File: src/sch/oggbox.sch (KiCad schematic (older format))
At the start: 146 parts, among them IC1 VS1053, IC2 MCP73831T, IC3 SD_CARD, IC4 MCP1802T-3002I-OT, IC5 STM32F103RBT, IC7 TPS76318, IC8 TPS76328, IC9 MCP102, P10 PHONES, P2 USB, P5 CONN_4, P6 CONN_28, P7 FTDI, P8 JTAG, P9 LINE, Q1 BC817, Q2 BC817, Q3 BSH121, Q4 BSH121, Q5 BSH121, SW1 VOL_UP, SW10 UP, SW11 HOLD, SW2 VOL_DN, SW3 RESET, SW4 MENU, SW5 SET, SW7 DOWN, SW8 LEFT, SW9 RIGHT, X1 12.288MHz, X2 32768Hz, X3 8MHz

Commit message: Routed the new volume switches
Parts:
- removed SW1: VOL_UP, SW_B3U-3000P-B, symbol SW_PUSH
- removed SW2: VOL_DN, SW_B3U-3000P-B, symbol SW_PUSH
- removed SW3: RESET, SW_B3U-3000P-B, symbol SW_PUSH
- added SW1: VOL_UP, symbol SW_PUSH4
- added SW2: VOL_DN, symbol SW_PUSH4
- added SW3: RESET, symbol SW_PUSH4
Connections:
- wire segments 526 -> 536
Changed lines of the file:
@@
-EESchema Schematic File Version 2  date Sat 22 Sep 2012 20:59:45 BST
+EESchema Schematic File Version 2  date Sun 23 Sep 2012 13:00:38 BST
 LIBS:power
 LIBS:device
@@
 Sheet 1 1
 Title "OggBox open hardware media player"
-Date "22 sep 2012"
+Date "23 sep 2012"
 Rev "B"
 Comp "nathandumont.com"
@@
 Comment4 ""
 $EndDescr
-Text Label 10250 10500 1    60   ~ 0
-RBG
+Wire Wire Line
+	8250 2700 8650 2700
+Wire Wire Line
+	8250 2700 8250 2600
+Connection ~ 5500 4050
+Wire Wire Line
+	5500 4050 5500 3950
+Wire Wire Line
+	5500 3950 5600 3950
+Connection ~ 6300 4150
+Wire Wire Line
+	6200 4250 6300 4250
+Wire Wire Line
+	6300 4250 6300 4150
 Wire Wire Line
 	10250 10300 10250 10550
@@
 	8350 2600 8350 2800
 Wire Wire Line
-	8350 2700 8650 2700
-Wire Wire Line
 	8650 2700 8650 2450
 Connection ~ 8350 1900
@@
 	8350 2000 8350 1800
 Wire Wire Line
-	8350 1900 9550 1900
-Wire Wire Line
-	9550 1900 9550 2650
+	9550 2650 9550 1900
 Connection ~ 8650 1900
 Wire Wire Line
@@
 Wire Wire Line
 	10250 9700 9350 9700
+Wire Wire Line
+	6200 3950 6300 3950
+Wire Wire Line
+	6300 3950 6300 4050
+Connection ~ 6300 4050
+Wire Wire Line
+	5500 4150 5500 4250
+Wire Wire Line
+	5500 4250 5600 4250
+Connection ~ 5500 4150
+Wire Wire Line
+	9550 1900 8250 1900
+Wire Wire Line
+	8250 1900 8250 2000
+$Comp
+L SW_PUSH4 SW3
+U 1 1 505EF9B9
+P 8300 2300
+F 0 "SW3" H 8450 2460 50  0000 C CNN
+F 1 "RESET" H 8300 2170 50  0000 C CNN
+	1    8300 2300
+	0    -1   -1   0
+$EndComp
+$Comp
+L SW_PUSH4 SW?
+U 1 1 505EF927
+P 5900 4000
+AR Path="/505EF91E" Ref="SW?"  Part="1"
+AR Path="/505EF927" Ref="SW1"  Part="1"
+F 0 "SW1" H 5550 4100 50  0000 C CNN
+F 1 "VOL_UP" H 6300 4100 50  0000 C CNN
+	1    5900 4000
+	1    0    0    -1
+$EndComp
+$Comp
+L SW_PUSH4 SW2
+U 1 1 505EF91E
+P 5900 4200
+F 0 "SW2" H 6050 4360 50  0000 C CNN
+F 1 "VOL_DN" H 5700 4350 50  0000 C CNN
+	1    5900 4200
+	1    0    0    1
+$EndComp
+Text Label 10250 10500 1    60   ~ 0
+RBG
 $Comp
 L C C?
@@
 U 1 1 4F3E5CAC
 P 5700 3650
-F 0 "D1" V 5450 3650 60  0000 C CNN
+F 0 "D1" V 5700 3850 60  0000 C CNN
 F 1 "LED_RG" V 5950 3650 60  0000 C CNN
 F 2 "SOT23" V 6050 3650 60  0001 C CNN
@@
 $EndComp
 $Comp
-L SW_PUSH SW3
-U 1 1 4D36058B
-P 8350 2300
-F 0 "SW3" H 8500 2410 50  0000 C CNN
-F 1 "RESET" H 8350 2220 50  0000 C CNN
-F 2 "SW_B3U-3000P-B" H 8350 2320 50  0001 C CNN
-F 4 "9962859" H 8350 2300 60  0001 C CNN "Farnell"
-	1    8350 2300
-	0    -1   -1   0
-$EndComp
-$Comp
 L R R?
 U 1 1 4D36040D
@@
 	1    0    0    -1
 $EndComp
-$Comp
-L SW_PUSH SW2
-U 1 1 4D35AE93
-P 5900 4150
-F 0 "SW2" H 6200 4200 50  0000 C CNN
-F 1 "VOL_DN" H 5500 4200 50  0000 C CNN
-F 2 "SW_B3U-3000P-B" H 5500 4300 50  0001 C CNN
-F 4 "9962859" H 5900 4150 60  0001 C CNN "Farnell"
-	1    5900 4150
-	1    0    0    -1
-$EndComp
-$Comp
-L SW_PUSH SW1
-U 1 1 4D35AE8C
-P 5900 4050
-F 0 "SW1" H 6200 4100 50  0000 C CNN
-F 1 "VOL_UP" H 5500 4100 50  0000 C CNN
-F 2 "SW_B3U-3000P-B" H 5500 4200 50  0001 C CNN
-F 4 "9962859" H 5900 4050 60  0001 C CNN "Farnell"
-	1    5900 4050
-	1    0    0    -1
-$EndComp

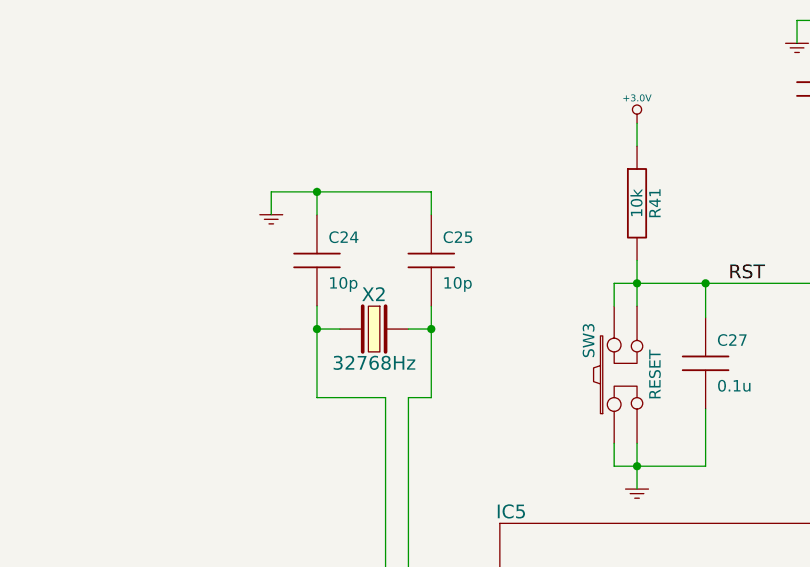
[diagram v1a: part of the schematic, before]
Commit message: Changed the footprint of the RTC crystal to an SMD part
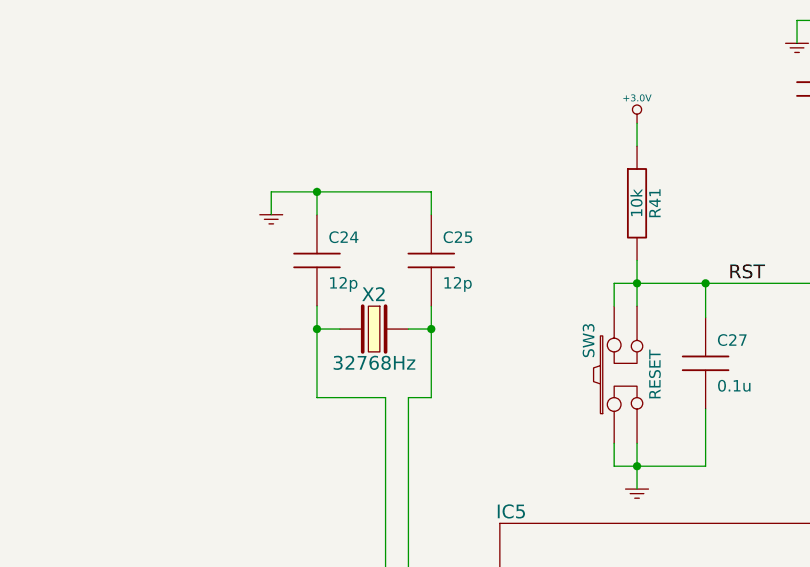
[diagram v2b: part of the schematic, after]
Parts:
- C24, C25: value 10p -> 12p
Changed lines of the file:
@@
-EESchema Schematic File Version 2  date Sun 23 Sep 2012 13:00:38 BST
+EESchema Schematic File Version 2  date Sun 23 Sep 2012 15:55:00 BST
 LIBS:power
 LIBS:device
@@
 AR Path="/4D35FD0D" Ref="C25"  Part="1"
 F 0 "C25" H 7500 1900 50  0000 L CNN
-F 1 "10p" H 7500 1700 50  0000 L CNN
+F 1 "12p" H 7500 1700 50  0000 L CNN
 F 2 "SM0805" H 7500 1800 50  0001 C CNN
 	1    7450 1800
@@
 P 6950 1800
 F 0 "C24" H 7000 1900 50  0000 L CNN
-F 1 "10p" H 7000 1700 50  0000 L CNN
+F 1 "12p" H 7000 1700 50  0000 L CNN
 F 2 "SM0805" H 7000 1800 50  0001 C CNN
 	1    6950 1800

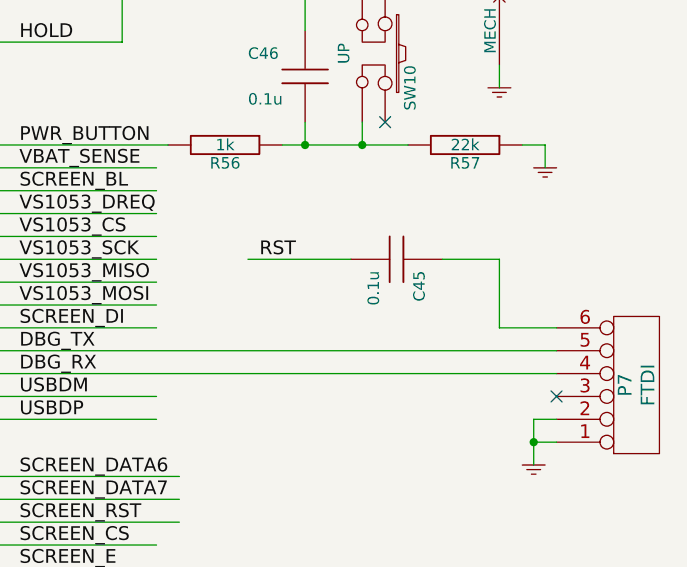
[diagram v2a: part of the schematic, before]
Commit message: Moving stuff around to try and shift the SD socket
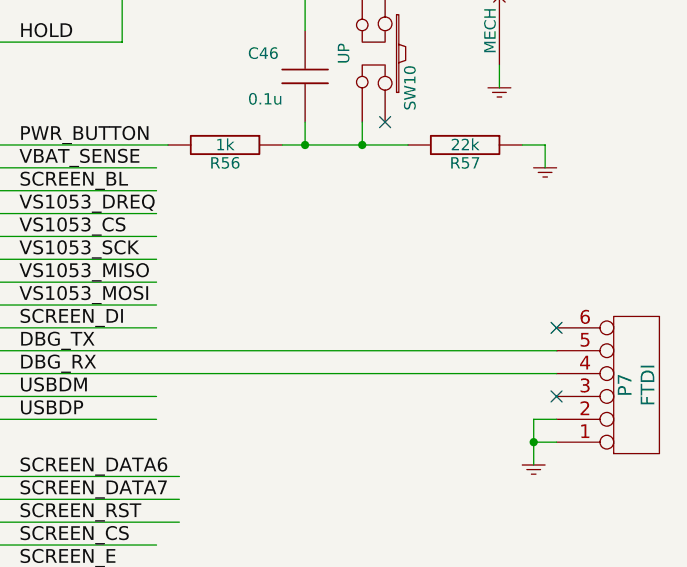
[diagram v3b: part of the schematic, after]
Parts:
- removed C45: 0.1u, SM0805, symbol C
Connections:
- wire segments 536 -> 532
- no-connect marks 19 -> 20
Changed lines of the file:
@@
-EESchema Schematic File Version 2  date Sun 23 Sep 2012 15:55:00 BST
+EESchema Schematic File Version 2  date Mon 24 Sep 2012 12:49:30 BST
+LIBS:74xx
+LIBS:adc-dac
+LIBS:analog_switches
+LIBS:atmel
+LIBS:audio
+LIBS:cmos4000
+LIBS:conn
+LIBS:contrib
+LIBS:cypress
+LIBS:dev_boards
+LIBS:device
+LIBS:digital-audio
+LIBS:display
+LIBS:dsp
+LIBS:intel
+LIBS:interface
+LIBS:linear
+LIBS:maxim
+LIBS:memory
+LIBS:microchip
+LIBS:microcontrollers
+LIBS:motorola
+LIBS:parallax
+LIBS:philips
 LIBS:power
-LIBS:device
+LIBS:regul
+LIBS:siliconi
+LIBS:special
+LIBS:texas
 LIBS:transistors
-LIBS:conn
-LIBS:linear
-LIBS:regul
-LIBS:74xx
-LIBS:cmos4000
-LIBS:adc-dac
-LIBS:memory
+LIBS:valves
 LIBS:xilinx
-LIBS:special
-LIBS:microcontrollers
-LIBS:dsp
-LIBS:microchip
-LIBS:analog_switches
-LIBS:motorola
-LIBS:texas
-LIBS:intel
-LIBS:audio
-LIBS:interface
-LIBS:digital-audio
-LIBS:philips
-LIBS:display
-LIBS:cypress
-LIBS:siliconi
-LIBS:opto
-LIBS:atmel
-LIBS:contrib
-LIBS:valves
 LIBS:oggbox-cache
 EELAYER 25  0
@@
 Sheet 1 1
 Title "OggBox open hardware media player"
-Date "23 sep 2012"
+Date "24 sep 2012"
 Rev "B"
 Comp "nathandumont.com"
@@
 Comment4 ""
 $EndDescr
+NoConn ~ 15500 4350
 Wire Wire Line
 	8250 2700 8650 2700
@@
 Wire Wire Line
 	13050 4550 15500 4550
-Wire Wire Line
-	15500 4350 15250 4350
-Wire Wire Line
-	15250 4350 15250 4050
-Wire Wire Line
-	15250 4050 15000 4050
 Wire Wire Line
 	6500 4900 6500 4800
@@
 Wire Wire Line
 	4300 3350 4300 3550
-Wire Wire Line
-	14600 4050 14150 4050
 Connection ~ 15400 4850
 Wire Wire Line
@@
 	1    0    0    -1
 $EndComp
-Text Label 14200 4050 0    60   ~ 0
-RST
-$Comp
-L C C45
-U 1 1 4F3E4BD3
-P 14800 4050
-F 0 "C45" H 14850 4150 50  0000 L CNN
-F 1 "0.1u" H 14850 3950 50  0000 L CNN
-F 2 "SM0805" H 14850 4050 50  0001 C CNN
-	1    14800 4050
-	0    1    1    0
-$EndComp
 NoConn ~ 15500 4650

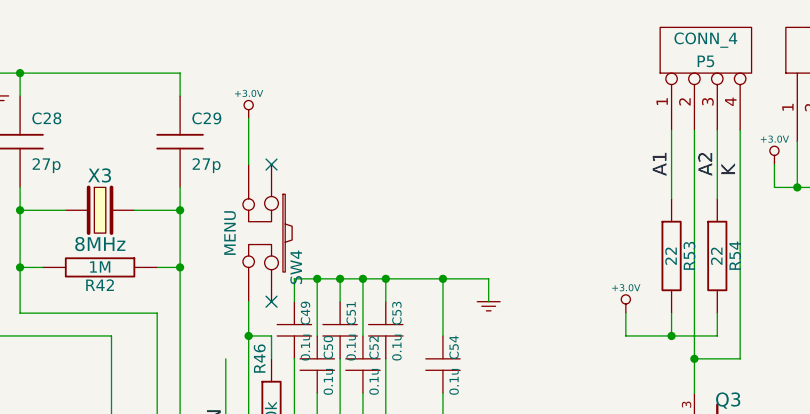
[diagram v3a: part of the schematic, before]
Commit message: Added extra decoupling and updated silkscreen
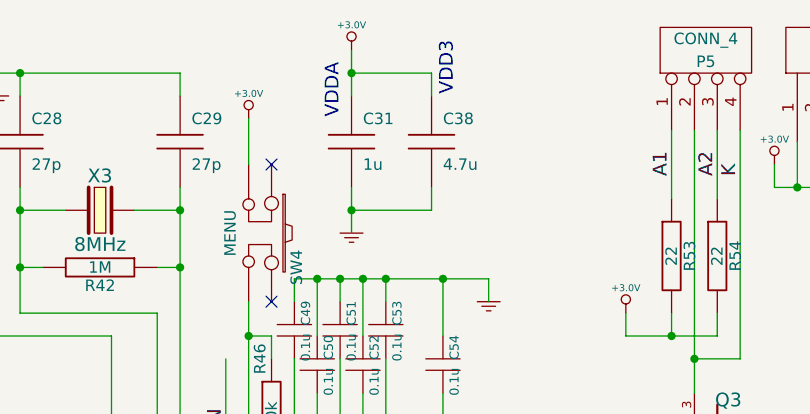
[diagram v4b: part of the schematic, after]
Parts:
- added C31: 1u, symbol C
- added C38: 4.7u, symbol C
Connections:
- wire segments 532 -> 538
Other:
- note added: "VDD3"
- note added: "VDDA"

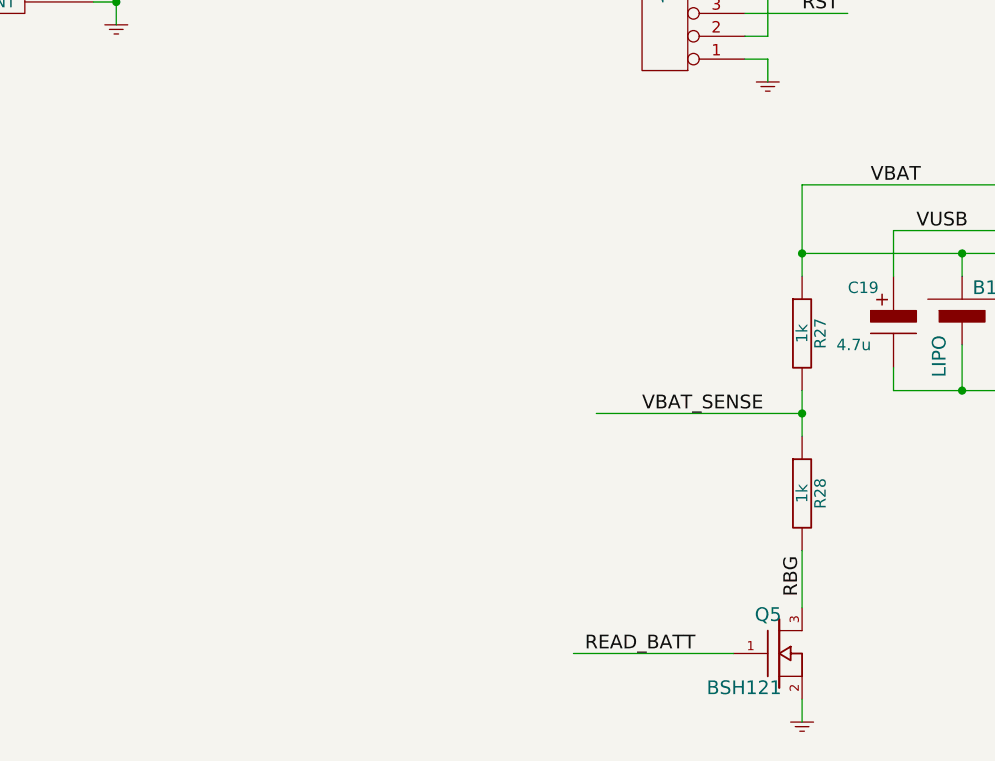
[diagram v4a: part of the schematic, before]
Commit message: Started the Rev C schematic, just changed the battery voltage check switch to a P type MOSFET
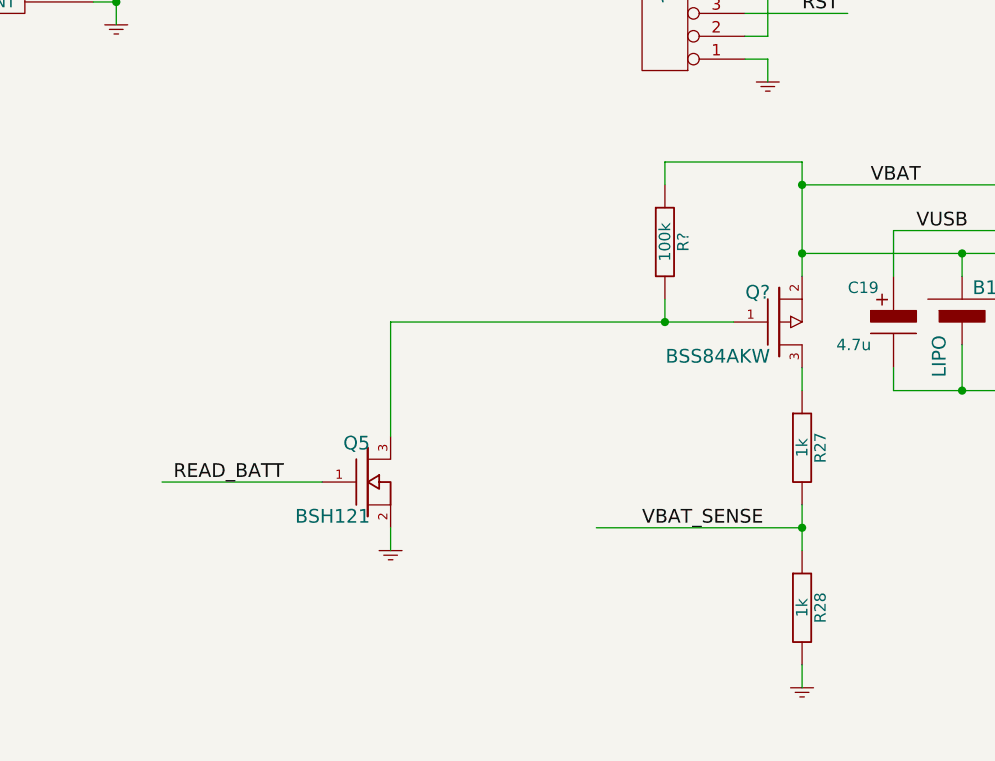
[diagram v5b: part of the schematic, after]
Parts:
- added Q?: BSS84AKW, ~, symbol BSS84AKW
- added R?: 100k, ~, symbol R
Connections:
- net labels removed: RBG
- wire segments 538 -> 544
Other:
- moved on the sheet: Q5, R27, R28
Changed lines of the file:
@@
-EESchema Schematic File Version 2  date Mon 24 Sep 2012 22:22:54 BST
-LIBS:power
-LIBS:device
-LIBS:transistors
-LIBS:conn
-LIBS:linear
-LIBS:regul
+EESchema Schematic File Version 2  date Fri 22 Feb 2013 22:14:53 GMT
 LIBS:74xx
-LIBS:cmos4000
 LIBS:adc-dac
-LIBS:memory
-LIBS:xilinx
-LIBS:special
-LIBS:microcontrollers
-LIBS:dsp
-LIBS:microchip
 LIBS:analog_switches
-LIBS:motorola
-LIBS:texas
-LIBS:intel
+LIBS:atmel
 LIBS:audio
-LIBS:interface
+LIBS:cmos4000
+LIBS:conn
+LIBS:contrib
+LIBS:cypress
+LIBS:dev_boards
+LIBS:device
 LIBS:digital-audio
-LIBS:philips
 LIBS:display
-LIBS:cypress
+LIBS:dsp
+LIBS:intel
+LIBS:interface
+LIBS:linear
+LIBS:maxim
+LIBS:memory
+LIBS:microchip
+LIBS:microcontrollers
+LIBS:motorola
+LIBS:parallax
+LIBS:philips
+LIBS:power
+LIBS:regul
+LIBS:rf
 LIBS:siliconi
-LIBS:opto
-LIBS:atmel
-LIBS:contrib
+LIBS:special
+LIBS:texas
+LIBS:transistors
 LIBS:valves
+LIBS:xilinx
 LIBS:oggbox-cache
-EELAYER 25  0
+EELAYER 27 0
 EELAYER END
-$Descr A3 16535 11700
+$Descr A3 16535 11693
 encoding utf-8
 Sheet 1 1
 Title "OggBox open hardware media player"
-Date "24 sep 2012"
+Date "22 feb 2013"
 Rev "B"
 Comp "nathandumont.com"
@@
 Wire Wire Line
 	6300 4250 6300 4150
-Wire Wire Line
-	10250 10300 10250 10550
 Connection ~ 13550 7000
 Wire Wire Line
@@
 	15350 1250 15250 1250
 Wire Wire Line
-	10250 11050 10250 10950
+	8450 10300 8450 10200
 Connection ~ 12600 2350
 Wire Wire Line
@@
 Wire Wire Line
 	12700 8900 13200 8900
-Connection ~ 10250 9700
+Connection ~ 10250 10200
 Wire Wire Line
-	10250 9600 10250 9800
+	10250 10100 10250 10300
 Connection ~ 7450 6400
 Wire Wire Line
@@
 Connection ~ 7250 7600
 Wire Wire Line
-	10250 8700 10250 9100
+	10250 8600 10250 9100
 Wire Wire Line
 	5300 4150 5300 3950
@@
 	13300 2550 13300 2650
 Wire Wire Line
-	9950 10750 9250 10750
+	8150 10000 7450 10000
 Wire Wire Line
 	15350 1850 15350 1950
@@
 	13550 7000 14300 7000
 Wire Wire Line
-	10250 9700 9350 9700
+	10250 10200 9350 10200
 Wire Wire Line
 	6200 3950 6300 3950
@@
 	1    0    0    1
 $EndComp
-Text Label 10250 10500 1    60   ~ 0
-RBG
 $Comp
 L C C?
@@
 	1    0    0    -1
 $EndComp
-Text Label 9300 10750 0    60   ~ 0
+Text Label 7500 10000 0    60   ~ 0
 READ_BATT
 $Comp
 L BSH121 Q5
 U 1 1 500029A8
-P 10150 10750
-F 0 "Q5" H 10160 10920 60  0000 R CNN
-F 1 "BSH121" H 10160 10600 60  0000 R CNN
-	1    10150 10750
+P 8350 10000
+F 0 "Q5" H 8360 10170 60  0000 R CNN
+F 1 "BSH121" H 8360 9850 60  0000 R CNN
+	1    8350 10000
 	1    0    0    -1
 $EndComp
@@
 Text Label 12750 8900 0    60   ~ 0
 CHG_STAT
-Text Label 9550 9700 0    60   ~ 0
+Text Label 9550 10200 0    60   ~ 0
 VBAT_SENSE
 $Comp
 L GND #PWR071
 U 1 1 4D361C67
-P 10250 11050
-F 0 "#PWR071" H 10250 11050 30  0001 C CNN
-F 1 "GND" H 10250 10980 30  0001 C CNN
-	1    10250 11050
+P 8450 10300
+F 0 "#PWR071" H 8450 10300 30  0001 C CNN
+F 1 "GND" H 8450 10230 30  0001 C CNN
+	1    8450 10300
 	1    0    0    -1
 $EndComp
@@
 L R R28
 U 1 1 4D361C30
-P 10250 10050
-F 0 "R28" V 10330 10050 50  0000 C CNN
-F 1 "1k" V 10250 10050 50  0000 C CNN
-F 2 "SM0805" V 10350 10050 50  0001 C CNN
-	1    10250 10050
+P 10250 10550
+F 0 "R28" V 10330 10550 50  0000 C CNN
+F 1 "1k" V 10250 10550 50  0000 C CNN
+F 2 "SM0805" V 10350 10550 50  0001 C CNN
+	1    10250 10550
 	1    0    0    -1
 $EndComp
@@
 L R R27
 U 1 1 4D361C10
-P 10250 9350
-F 0 "R27" V 10330 9350 50  0000 C CNN
-F 1 "1k" V 10250 9350 50  0000 C CNN
-F 2 "SM0805" V 10350 9350 50  0001 C CNN
-	1    10250 9350
+P 10250 9850
+F 0 "R27" V 10330 9850 50  0000 C CNN
+F 1 "1k" V 10250 9850 50  0000 C CNN
+F 2 "SM0805" V 10350 9850 50  0001 C CNN
+	1    10250 9850
 	1    0    0    -1
 $EndComp
@@
 Text Label 6700 5150 0    60   ~ 0
 SCREEN_DATA0
+Wire Wire Line
+	10250 10900 10250 10800
+$Comp
+L GND #PWR?
+U 1 1 5127F00E
+P 10250 10900
+F 0 "#PWR?" H 10250 10900 30  0001 C CNN
+F 1 "GND" H 10250 10830 30  0001 C CNN
+	1    10250 10900
+	1    0    0    -1
+$EndComp
+$Comp
+L BSS84AKW Q?
+U 1 1 5127F37D
+P 10150 9300
+F 0 "Q?" H 10110 9430 60  0000 R CNN
+F 1 "BSS84AKW" H 10110 9150 60  0000 R CNN
+F 2 "~" H 10150 9300 60  0000 C CNN
+F 3 "~" H 10150 9300 60  0000 C CNN
+	1    10150 9300
+	1    0    0    -1
+$EndComp
+Wire Wire Line
+	10250 9500 10250 9600
+Wire Wire Line
+	9950 9300 8450 9300
+Wire Wire Line
+	8450 9300 8450 9800
+Wire Wire Line
+	9650 9300 9650 9200
+Connection ~ 9650 9300
+$Comp
+L R R?
+U 1 1 5127FBD4
+P 9650 8950
+F 0 "R?" V 9730 8950 50  0000 C CNN
+F 1 "100k" V 9650 8950 50  0000 C CNN
+F 2 "~" H 9650 8950 60  0000 C CNN
+F 3 "~" H 9650 8950 60  0000 C CNN
+	1    9650 8950
+	1    0    0    -1
+$EndComp
+Wire Wire Line
+	9650 8700 9650 8600
+Wire Wire Line
+	9650 8600 10250 8600
+Connection ~ 10250 8700
 $EndSCHEMATC

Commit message: Started laying out the Rev C board
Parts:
- removed C49, C50, C51, C52, C53, C54: 0.1u, SM0805, symbol CS
- removed IC5: STM32F103RBT, LQFP64, symbol STM32F103RBT
- removed R44: 10k, SM0805, symbol R
- added C49, C50, C51, C52, C53, C54: 0.1u, ~, symbol C
- added IC5: STM32F103RET, ~, symbol STM32F103RET
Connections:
- net labels added: +3.0VSB, +BATT, CHG_100, CHG_500, DOWN_BTN, LEFT_BTN, MENU_BTN, RIGHT_BTN, SCREEN_MOSI, SCREEN_SCK, SET_BTN
- net labels removed: VBAT
- wire segments 544 -> 551
- no-connect marks 20 -> 18
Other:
- note removed: "VDD3"
- note removed: "VDDA"
- moved on the sheet: B1, C1, C10, C11, C12, C13, C14, C15, C16, C17, C18, C19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

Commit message: Made some more schematic revisions for the Rev C
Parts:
- removed C42: 0.1u, SM0805, symbol CS
- added C42: 100nF, ~, symbol C
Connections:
- net labels added: AUX_PWR, SCREEN_A0
- net labels removed: CHG_FAST, SCREEN_DATA0, SCREEN_DATA1, SCREEN_DATA2, SCREEN_DATA3, SCREEN_DATA4, SCREEN_DATA5, SCREEN_DATA6, SCREEN_DATA7, SCREEN_DI, SCREEN_E, SCREEN_RW
- wire segments 551 -> 538
- no-connect marks 18 -> 19
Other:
- moved on the sheet: P7, R32, R34, SW1, SW2

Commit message: Oggbox Rev C almost ready to order!
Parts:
- removed B1: LIPO, JUMPER, symbol CELL
- removed P8: JTAG, header_smd, symbol CONN_8
- removed Q1, Q2: BC817, SOT23, symbol BC817
- removed X1: 12.288MHz, HC49SM, symbol CRYSTAL
- removed X3: 8MHz, HC49SM, symbol CRYSTAL
- added C45, C56, C57, C58, C59, C60, C61: 100nF, symbol C
- added C62, C63: 4.7uF, symbol C
- added IC6: MCP1802T-3002I-OT, symbol MCP1802T-3002I-OT
- added P1: CONN_3, symbol CONN_3
- added Q1, Q2: BSH121, symbol BSH121
- added R44, R59, R60, R61: 1k, symbol R
- added R62, R63, R64, R66: 100k, symbol R
- added R65: 1M, symbol R
- added X1: 12.288MHz, symbol CRYSTAL_SMD
- added X3: 8MHz, symbol CRYSTAL_SMD
- C1, C2: value 18p -> 18pF
- C10, C11, C12, C13, C14, C15, C16, C17, C27, C32, C33, C34, C35, C36, C46, C49, C50, C51, C52, C53, C54, C55, C8, C9: value 0.1u -> 100nF
- C18: value 0.047u -> 47nF
- C19, C22, C26, C30, C38, C47, C48: value 4.7u -> 4.7uF
- C20, C21, C5, C6: value 0.01u -> 10nF
- C23: value 47u -> 47uF
- C24, C25: value 12p -> 12pF
- C28, C29: value 27p -> 27pF
- C3, C31, C4, C43, C44, C7: value 1u -> 1uF
- C37, C39, C40, C41: value 2.2u -> 2.2uF
- R27, R28: value 1k -> 10k
- R32, R34, R48: value 10k -> 1k; footprint SM0805 -> (none)
- R49, R50, R51, R52: value 10k -> 100k; footprint SM0805 -> (none)
- gave numbers to parts that had none: 2
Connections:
- net labels added: +5VUSB
- net labels removed: VUSB
- wire segments 538 -> 583
- no-connect marks 19 -> 29
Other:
- note added: "Battery management"
- note added: "Buttons"
- note added: "CODEC Chip"
- note added: "Power Supply"
- note added: "Processor"
- note added: "SD Card"
- note added: "Screen"
- note added: "USB Connector"
- moved on the sheet: C1, C10, C11, C12, C13, C14, C15, C16, C17, C18, C19, C2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
